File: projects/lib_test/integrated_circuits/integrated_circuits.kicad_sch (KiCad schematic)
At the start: 2 parts, among them U1001 LM393, U1002 AZ1117

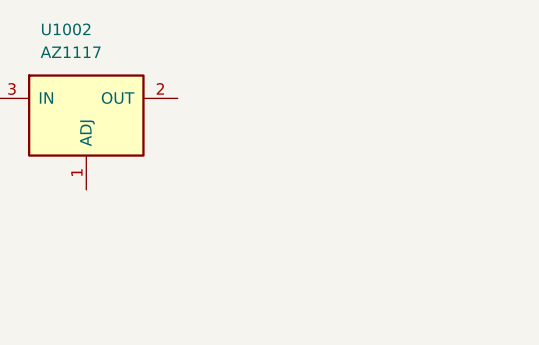
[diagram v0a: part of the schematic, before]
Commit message: add regulator TPS5430
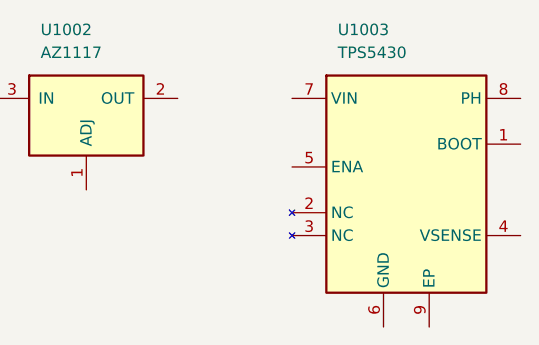
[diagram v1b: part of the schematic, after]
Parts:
- added U1003: TPS5430, lily_footprints:hsoic8, symbol lily_symbols:ic_volt_reg_switching_TPS5430_hsoic8
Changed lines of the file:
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@@
+	)
+	(symbol
+		(lib_id "lily_symbols:ic_volt_reg_switching_TPS5430_hsoic8")
+		(at 147.32 38.1 0)
+		(unit 1)
+		(exclude_from_sim no)
+		(in_bom yes)
+		(on_board yes)
+		(dnp no)
+		(property "Reference" "U1003"
+			(at 152.4 30.48 0)
+			(effects
+				(font
+					(size 1.27 1.27)
+				)
+				(justify left)
+			)
+		)
+		(property "Value" "TPS5430"
+			(at 152.4 33.02 0)
+			(effects
+				(font
+					(size 1.27 1.27)
+				)
+				(justify left)
+			)
+		)
+		(property "Footprint" "lily_footprints:hsoic8"
+			(at 160.02 81.28 0)
+			(effects
+				(font
+					(size 1.27 1.27)
+				)
+				(hide yes)
+			)
+		)
+		(property "Datasheet" ""
+			(at 147.32 38.1 0)
+			(effects
+				(font
+					(size 1.27 1.27)
+				)
+				(hide yes)
+			)
+		)
+		(property "Description" ""
+			(at 147.32 38.1 0)
+			(effects
+				(font
+					(size 1.27 1.27)
+				)
+				(hide yes)
+			)
+		)
+		(property "Revision" "1"
+			(at 160.02 76.2 0)
+			(effects
+				(font
+					(size 1.27 1.27)
+				)
+				(hide yes)
+			)
+		)
+		(property "Status" "Active"
+			(at 160.02 78.74 0)
+			(effects
+				(font
+					(size 1.27 1.27)
+				)
+				(hide yes)
+			)
+		)
+		(property "Manufacturer" "Texas Instruments"
+			(at 160.02 83.82 0)
+			(effects
+				(font
+					(size 1.27 1.27)
+				)
+				(hide yes)
+			)
+		)
+		(property "Manufacturer_ID" "TPS5430DDA"
+			(at 160.02 86.36 0)
+			(effects
+				(font
+					(size 1.27 1.27)
+				)
+				(hide yes)
+			)
+		)
+		(property "Lily_ID" "xxxx-yyyyy"
+			(at 160.02 88.9 0)
+			(effects
+				(font
+					(size 1.27 1.27)
+				)
+				(hide yes)
+			)
+		)
+		(property "JLCPCB_ID" "C9864"
+			(at 160.02 91.44 0)
+			(effects
+				(font
+					(size 1.27 1.27)
+				)
+				(hide yes)
+			)
+		)
+		(property "JLCPCB_STATUS" "Basic"
+			(at 160.02 93.98 0)
+			(effects
+				(font
+					(size 1.27 1.27)
+				)
+				(hide yes)
+			)
+		)
+		(pin "3"
+		)
+		(pin "7"
+		)
+		(pin "5"
+		)
+		(pin "2"
+		)
+		(pin "8"
+		)
+		(pin "6"
+		)
+		(pin "1"
+		)
+		(pin "9"
+		)
+		(pin "4"
+		)
+		(instances
+			(project ""
+				(path "/e63e39d7-6ac0-4ffd-8aa3-1841a4541b55"
+					(reference "U1003")
+					(unit 1)
+				)
+			)
+		)
 	)
 	(symbol

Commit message: updated test projects
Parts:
- removed U1002: AZ1117, lily_footprints:sot223, symbol lily_symbols:ic_volt_reg_AZ1117_sot223
- U1001: JLCPCB_STATUS Basic -> (none); Lily_ID 1914-10007 -> NO_ID; Notes Extended: C67470, is much cheaper -> (none)
- U1002: renamed from U1003; JLCPCB_STATUS Basic -> (none); Lily_ID xxxx-yyyyy -> NO_ID; Manufacturer_ID TPS5430DDA -> TPS5430DDAR
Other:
- moved on the sheet: U1002
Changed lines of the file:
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@@
 			)
 		)
-		(property "Datasheet" ""
-			(at 38.1 38.1 0)
+		(property "Datasheet" "https://lilytronics.github.io/lily_kicad_lib/datasheets/onsemi/LM393D.pdf"
+			(at 45.72 66.04 0)
 			(effects
 				(font
@@
 			)
 		)
-		(property "Lily_ID" "1914-10007"
+		(property "Lily_ID" "NO_ID"
 			(at 45.72 60.96 0)
 			(effects
@@
 		(property "JLCPCB_ID" "C7955"
 			(at 45.72 63.5 0)
-			(effects
-				(font
-					(size 1.27 1.27)
-				)
-				(hide yes)
-			)
-		)
-		(property "JLCPCB_STATUS" "Basic"
-			(at 45.72 66.04 0)
-			(effects
-				(font
-					(size 1.27 1.27)
-				)
-				(hide yes)
-			)
-		)
-		(property "Notes" "Extended: C67470, is much cheaper"
-			(at 45.72 68.58 0)
 			(effects
 				(font
@@
 				(path "/e63e39d7-6ac0-4ffd-8aa3-1841a4541b55"
 					(reference "U1001")
-					(unit 1)
-				)
-			)
-		)
-	)
-	(symbol
-		(lib_id "lily_symbols:ic_volt_reg_AZ1117_sot223")
-		(at 114.3 38.1 0)
-		(unit 1)
-		(exclude_from_sim no)
-		(in_bom yes)
-		(on_board yes)
-		(dnp no)
-		(property "Reference" "U1002"
-			(at 119.38 30.48 0)
-			(effects
-				(font
-					(size 1.27 1.27)
-				)
-				(justify left)
-			)
-		)
-		(property "Value" "AZ1117"
-			(at 119.38 33.02 0)
-			(effects
-				(font
-					(size 1.27 1.27)
-				)
-				(justify left)
-			)
-		)
-		(property "Footprint" "lily_footprints:sot223"
-			(at 124.46 60.96 0)
-			(effects
-				(font
-					(size 1.27 1.27)
-				)
-				(hide yes)
-			)
-		)
-		(property "Datasheet" ""
-			(at 114.3 38.1 0)
-			(effects
-				(font
-					(size 1.27 1.27)
-				)
-				(hide yes)
-			)
-		)
-		(property "Description" ""
-			(at 114.3 38.1 0)
-			(effects
-				(font
-					(size 1.27 1.27)
-				)
-				(hide yes)
-			)
-		)
-		(property "Revision" "1"
-			(at 124.46 55.88 0)
-			(effects
-				(font
-					(size 1.27 1.27)
-				)
-				(hide yes)
-			)
-		)
-		(property "Status" "Active"
-			(at 124.46 58.42 0)
-			(effects
-				(font
-					(size 1.27 1.27)
-				)
-				(hide yes)
-			)
-		)
-		(property "Manufacturer" "Diodes Incorporated"
-			(at 124.46 63.5 0)
-			(effects
-				(font
-					(size 1.27 1.27)
-				)
-				(hide yes)
-			)
-		)
-		(property "Manufacturer_ID" "AZ1117CH-ADJTRG1"
-			(at 124.46 66.04 0)
-			(effects
-				(font
-					(size 1.27 1.27)
-				)
-				(hide yes)
-			)
-		)
-		(property "Lily_ID" "1914-10010"
-			(at 124.46 68.58 0)
-			(effects
-				(font
-					(size 1.27 1.27)
-				)
-				(hide yes)
-			)
-		)
-		(property "JLCPCB_ID" "C95398"
-			(at 124.46 71.12 0)
-			(effects
-				(font
-					(size 1.27 1.27)
-				)
-				(hide yes)
-			)
-		)
-		(property "JLCPCB_STATUS" "Extended"
-			(at 124.46 73.66 0)
-			(effects
-				(font
-					(size 1.27 1.27)
-				)
-				(hide yes)
-			)
-		)
-		(pin "3"
-		)
-		(pin "2"
-		)
-		(pin "1"
-		)
-		(instances
-			(project ""
-				(path "/e63e39d7-6ac0-4ffd-8aa3-1841a4541b55"
-					(reference "U1002")
 					(unit 1)
 				)
@@
 		(dnp no)
 		(property "Reference" "U1001"
+			(at 95.25 36.83 0)
+			(effects
+				(font
+					(size 1.27 1.27)
+				)
+				(justify left)
+			)
+		)
+		(property "Value" "LM393"
 			(at 95.25 39.37 0)
-			(effects
-				(font
-					(size 1.27 1.27)
-				)
-				(justify left)
-			)
-		)
-		(property "Value" "LM393"
-			(at 95.25 41.91 0)
 			(effects
 				(font
@@
 			)
 		)
-		(property "Datasheet" ""
-			(at 91.44 30.48 0)
+		(property "Datasheet" "https://lilytronics.github.io/lily_kicad_lib/datasheets/onsemi/LM393D.pdf"
+			(at 99.06 58.42 0)
 			(effects
 				(font
@@
 			)
 		)
-		(property "Lily_ID" "1914-10007"
+		(property "Lily_ID" "NO_ID"
 			(at 99.06 53.34 0)
 			(effects
@@
 		(property "JLCPCB_ID" "C7955"
 			(at 99.06 55.88 0)
-			(effects
-				(font
-					(size 1.27 1.27)
-				)
-				(hide yes)
-			)
-		)
-		(property "JLCPCB_STATUS" "Basic"
-			(at 99.06 58.42 0)
-			(effects
-				(font
-					(size 1.27 1.27)
-				)
-				(hide yes)
-			)
-		)
-		(property "Notes" "Extended: C67470, is much cheaper"
-			(at 99.06 60.96 0)
 			(effects
 				(font
@@
 	(symbol
 		(lib_id "lily_symbols:ic_volt_reg_switching_TPS5430_hsoic8")
-		(at 147.32 38.1 0)
+		(at 127 38.1 0)
 		(unit 1)
 		(exclude_from_sim no)
@@
 		(on_board yes)
 		(dnp no)
-		(property "Reference" "U1003"
-			(at 152.4 30.48 0)
+		(property "Reference" "U1002"
+			(at 132.08 30.48 0)
 			(effects
 				(font
@@
 		)
 		(property "Value" "TPS5430"
-			(at 152.4 33.02 0)
+			(at 132.08 33.02 0)
 			(effects
 				(font
@@
 		)
 		(property "Footprint" "lily_footprints:hsoic8"
-			(at 160.02 81.28 0)
-			(effects
-				(font
-					(size 1.27 1.27)
-				)
-				(hide yes)
-			)
-		)
-		(property "Datasheet" ""
-			(at 147.32 38.1 0)
+			(at 139.7 81.28 0)
+			(effects
+				(font
+					(size 1.27 1.27)
+				)
+				(hide yes)
+			)
+		)
+		(property "Datasheet" "https://lilytronics.github.io/lily_kicad_lib/datasheets/texas_instruments/TPS5430.pdf"
+			(at 139.7 93.98 0)
 			(effects
 				(font
@@
 		)
 		(property "Description" ""
-			(at 147.32 38.1 0)
+			(at 127 38.1 0)
 			(effects
 				(font
@@
 		)
 		(property "Revision" "1"
-			(at 160.02 76.2 0)
+			(at 139.7 76.2 0)
 			(effects
 				(font
@@
 		)
 		(property "Status" "Active"
-			(at 160.02 78.74 0)
+			(at 139.7 78.74 0)
 			(effects
 				(font
@@
 		)
 		(property "Manufacturer" "Texas Instruments"
-			(at 160.02 83.82 0)
-			(effects
-				(font
-					(size 1.27 1.27)
-				)
-				(hide yes)
-			)
-		)
-		(property "Manufacturer_ID" "TPS5430DDA"
-			(at 160.02 86.36 0)
-			(effects
-				(font
-					(size 1.27 1.27)
-				)
-				(hide yes)
-			)
-		)
-		(property "Lily_ID" "xxxx-yyyyy"
-			(at 160.02 88.9 0)
+			(at 139.7 83.82 0)
+			(effects
+				(font
+					(size 1.27 1.27)
+				)
+				(hide yes)
+			)
+		)
+		(property "Manufacturer_ID" "TPS5430DDAR"
+			(at 139.7 86.36 0)
+			(effects
+				(font
+					(size 1.27 1.27)
+				)
+				(hide yes)
+			)
+		)
+		(property "Lily_ID" "NO_ID"
+			(at 139.7 88.9 0)
 			(effects
 				(font
@@
 		)
 		(property "JLCPCB_ID" "C9864"
-			(at 160.02 91.44 0)
-			(effects
-				(font
-					(size 1.27 1.27)
-				)
-				(hide yes)
-			)
-		)
-		(property "JLCPCB_STATUS" "Basic"
-			(at 160.02 93.98 0)
+			(at 139.7 91.44 0)
 			(effects
 				(font
@@
 			(project ""
 				(path "/e63e39d7-6ac0-4ffd-8aa3-1841a4541b55"
-					(reference "U1003")
+					(reference "U1002")
 					(unit 1)
 				)
@@
 			)
 		)
-		(property "Datasheet" ""
-			(at 63.5 38.1 0)
+		(property "Datasheet" "https://lilytronics.github.io/lily_kicad_lib/datasheets/onsemi/LM393D.pdf"
+			(at 71.12 66.04 0)
 			(effects
 				(font
@@
 			)
 		)
-		(property "Lily_ID" "1914-10007"
+		(property "Lily_ID" "NO_ID"
 			(at 71.12 60.96 0)
 			(effects
@@
 			(effects
 				(font
-					(size 1.27 1.27)
-				)
-				(hide yes)
-			)
-		)
-		(property "JLCPCB_STATUS" "Basic"
-			(at 71.12 66.04 0)
-			(effects
-				(font
-					(size 1.27 1.27)
-				)
-				(hide yes)
-			)
-		)
-		(property "Notes" "Extended: C67470, is much cheaper"
-			(at 71.12 68.58 0)
-			(effects
-				(font

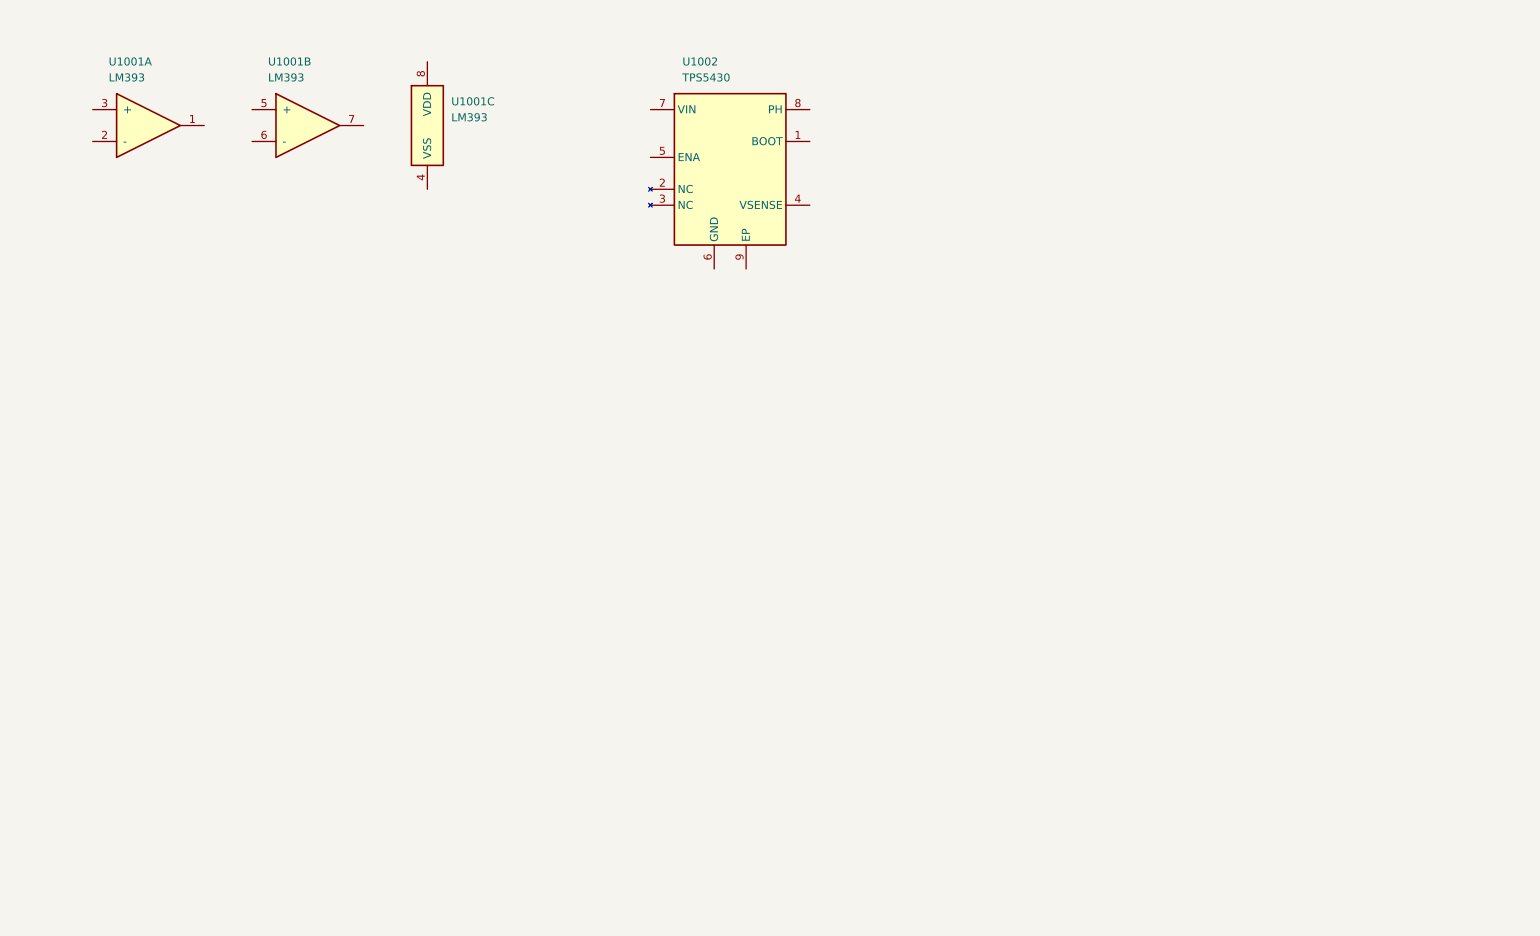
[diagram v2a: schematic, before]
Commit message: put all symbols in the test designs
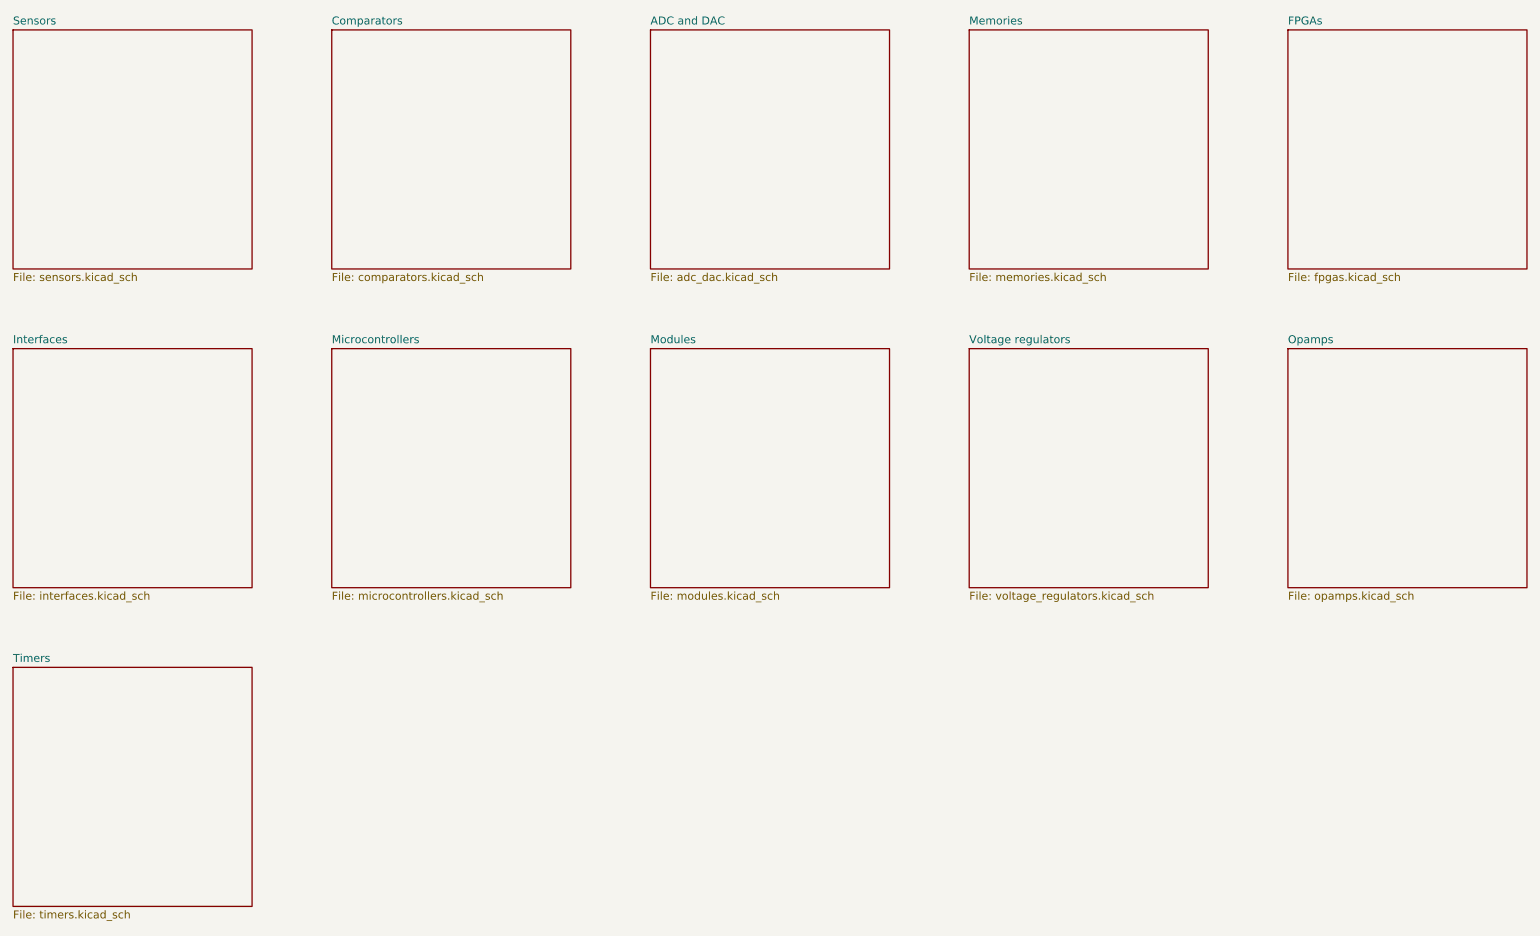
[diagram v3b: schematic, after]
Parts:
- removed U1001: LM393, lily_footprints:soic8, symbol lily_symbols:ic_comparator_dual_LM393_soic8
- removed U1002: TPS5430, lily_footprints:hsoic8, symbol lily_symbols:ic_volt_reg_switching_TPS5430_hsoic8
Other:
- added sheet ADC and DAC (adc_dac.kicad_sch)
- added sheet Comparators (comparators.kicad_sch)
- added sheet FPGAs (fpgas.kicad_sch)
- added sheet Interfaces (interfaces.kicad_sch)
- added sheet Memories (memories.kicad_sch)
- added sheet Microcontrollers (microcontrollers.kicad_sch)
- added sheet Modules (modules.kicad_sch)
- added sheet Opamps (opamps.kicad_sch)
- added sheet Sensors (sensors.kicad_sch)
- added sheet Timers (timers.kicad_sch)
- added sheet Voltage regulators (voltage_regulators.kicad_sch)
- title: Project name -> Integrated circuits

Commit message: updated test projects
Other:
- added sheet Battery chargers (battery_chargers.kicad_sch)
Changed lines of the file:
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@@
+	)
+	(sheet
+		(at 76.2 127)
+		(size 38.1 38.1)
+		(exclude_from_sim no)
+		(in_bom yes)
+		(on_board yes)
+		(dnp no)
+		(fields_autoplaced yes)
+		(stroke
+			(width 0.1524)
+			(type solid)
+		)
+		(fill
+			(color 0 0 0 0.0000)
+		)
+		(property "Sheetname" "Battery chargers"
+			(at 76.2 126.2884 0)
+			(effects
+				(font
+					(size 1.27 1.27)
+				)
+				(justify left bottom)
+			)
+		)
+		(property "Sheetfile" "battery_chargers.kicad_sch"
+			(at 76.2 165.6846 0)
+			(effects
+				(font
+					(size 1.27 1.27)
+				)
+				(justify left top)
+			)
+		)
+		(instances
+			(project "integrated_circuits"
+				(path "/e63e39d7-6ac0-4ffd-8aa3-1841a4541b55"
+					(page "13")
+				)
+			)
+		)
 	)
 	(sheet
